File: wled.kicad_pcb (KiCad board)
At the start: 2 copper layers, 310 x 282.6 mm, 12 parts, among them J0 Screw_Terminal_01x02, J1 Signal_Output_01, J3 1Wire_output_02, J4 1Wire_output_01, J5 I2C_output_01, SW1 Button_01, SW2 Button_Reset, U1 NodeMCU_1.0_(ESP-12E)

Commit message: feat: Updated PCB design
This is a Release Candidate version of the board. It still has some issues, and they will be fixed in the next commit
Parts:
- removed C1: Capacitor_1000μF, Capacitor_THT:CP_Radial_D10.0mm_P5.00mm
- J0: value Screw_Terminal_01x02 -> PinHeader_1x02_P2.54mm_Horizontal; footprint TerminalBlock:TerminalBlock_bornier-2_P5.08mm -> Connector_PinHeader_2.54mm:PinHeader_1x02_P2.54mm_Horizontal
- J1: value Signal_Output_01 -> PinHeader_1x03_P2.54mm_Horizontal; footprint TerminalBlock:TerminalBlock_bornier-3_P5.08mm -> Connector_PinHeader_2.54mm:PinHeader_1x03_P2.54mm_Horizontal
- R1: value Resistor_220kΩ -> 220kΩ
- R2: value Resistor_62Ω -> 62Ω
- SW1: value Button_01 -> SW_Push
- SW2: value Button_Reset -> SW_Push
- moved J0 97.9 mm to (82.5, 124.5), turned to 180 degrees
- moved J1 74.4 mm to (153.1, 105.4), turned to 0 degrees
- moved SW2 71.5 mm to (82.2, 115.0), turned to 90 degrees
- moved R1 69.3 mm to (80.6, 101.0), turned to 0 degrees
- moved R2 54.3 mm to (139.7, 105.4), turned to 0 degrees
- moved J4 53.0 mm to (82.6, 78.7), turned to 90 degrees
- moved C2 41.9 mm to (129.5, 109.2), turned to 0 degrees
- moved J3 39.7 mm to (82.6, 87.4), turned to 90 degrees
- moved J5 37.1 mm to (111.8, 85.1), turned to 90 degrees
- moved U1 33.5 mm to (105.4, 113.0), turned to 0 degrees
- moved SW1 31.7 mm to (128.6, 87.4)
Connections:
- net Net-(C2-Pad2) renamed SIG_OUT_3V3DC
- net Net-(C2-Pad8) renamed SIG_OUT_RAW
- net Net-(J5-Pad3) renamed I2C_SCL
- net Net-(J5-Pad4) renamed I2C_SDA
- net Net-(R1-Pad1) renamed RST_PUP
- net Net-(SW1-Pad2) renamed BTN_DATA
- C2 pad 10: Net-(C1-Pad2) -> GND
- C2 pad 3: Net-(C2-Pad3) -> 3V3DC
- C2 pad 4: Net-(C2-Pad4) -> GND
- C2 pad 9: Net-(C1-Pad1) -> 5VDC
- J0 pad 1: Net-(C1-Pad1) -> GND
- J0 pad 2: Net-(C1-Pad2) -> 5VDC
- J1 pad 1: Net-(C1-Pad1) -> GND
- J1 pad 2: Net-(J1-Pad2) -> 5VDC
- J1 pad 3: Net-(C1-Pad2) -> SIG_OUT_5VDC
- J3 pad 1: Net-(J3-Pad1) -> GND
- J3 pad 2: Net-(J3-Pad2) -> 3V3DC
- J3 pad 3: Net-(J3-Pad3) -> 1WIRE_02
- J4 pad 1: Net-(J3-Pad1) -> GND
- J4 pad 2: Net-(J4-Pad2) -> 3V3DC
- J4 pad 3: Net-(J3-Pad3) -> 1WIRE_01
- J5 pad 1: Net-(J3-Pad1) -> GND
- J5 pad 2: Net-(J3-Pad3) -> 3V3DC
- R1 pad 2: Net-(J3-Pad3) -> 3V3DC
- R2 pad 2: Net-(J1-Pad2) -> SIG_OUT_5VDC
- SW1 pad 1: Net-(J3-Pad3) -> 3V3DC
- SW2 pad 1: Net-(C1-Pad2) -> GND
- U1 pad 10: Net-(J3-Pad1) -> GND
- U1 pad 11: Net-(J3-Pad3) -> 3V3DC
- U1 pad 14: Net-(C1-Pad2) -> GND
- U1 pad 15: Net-(C1-Pad1) -> 5VDC
- U1 pad 17: unconnected-(U1-Pad17) -> GND
- U1 pad 2: unconnected-(U1-Pad2) -> GND
- U1 pad 24: Net-(C2-Pad4) -> GND
- U1 pad 25: Net-(C2-Pad3) -> 3V3DC
- U1 pad 4: Net-(J3-Pad2) -> 1WIRE_02
- U1 pad 5: Net-(J4-Pad2) -> 1WIRE_01
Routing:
- net 3V3DC: track 0.00 -> 122.4 mm
- net Net-(C1-Pad2): track 105.7 -> 0.00 mm
- net 5VDC: track 0.00 -> 94.9 mm
- net BTN_DATA: track 100.9 -> 11.0 mm
- net Net-(C1-Pad1): track 87.8 -> 0.00 mm
- net Net-(J3-Pad3): track 59.3 -> 0.00 mm
- net I2C_SDA: track 74.7 -> 18.1 mm
- net I2C_SCL: track 67.1 -> 16.6 mm
- net 1WIRE_01: track 0.00 -> 43.8 mm
- net Net-(J3-Pad1): track 41.0 -> 0.00 mm
- net 1WIRE_02: track 0.00 -> 26.3 mm
- net Net-(J3-Pad2): track 19.6 -> 0.00 mm
- net Net-(J4-Pad2): track 12.0 -> 0.00 mm
- net Net-(J1-Pad2): track 11.4 -> 0.00 mm
- net RST_PUP: track 12.3 -> 22.7 mm
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- added copper zone on F.Cu, net GND
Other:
- board size 310 x 282.6 mm -> 77.6 x 71.8 mm
- board text added: "sowi.tech ohw-wled v1.0-RC"
- board text removed: "sowi.tech WLED@ESP32 v0.1"

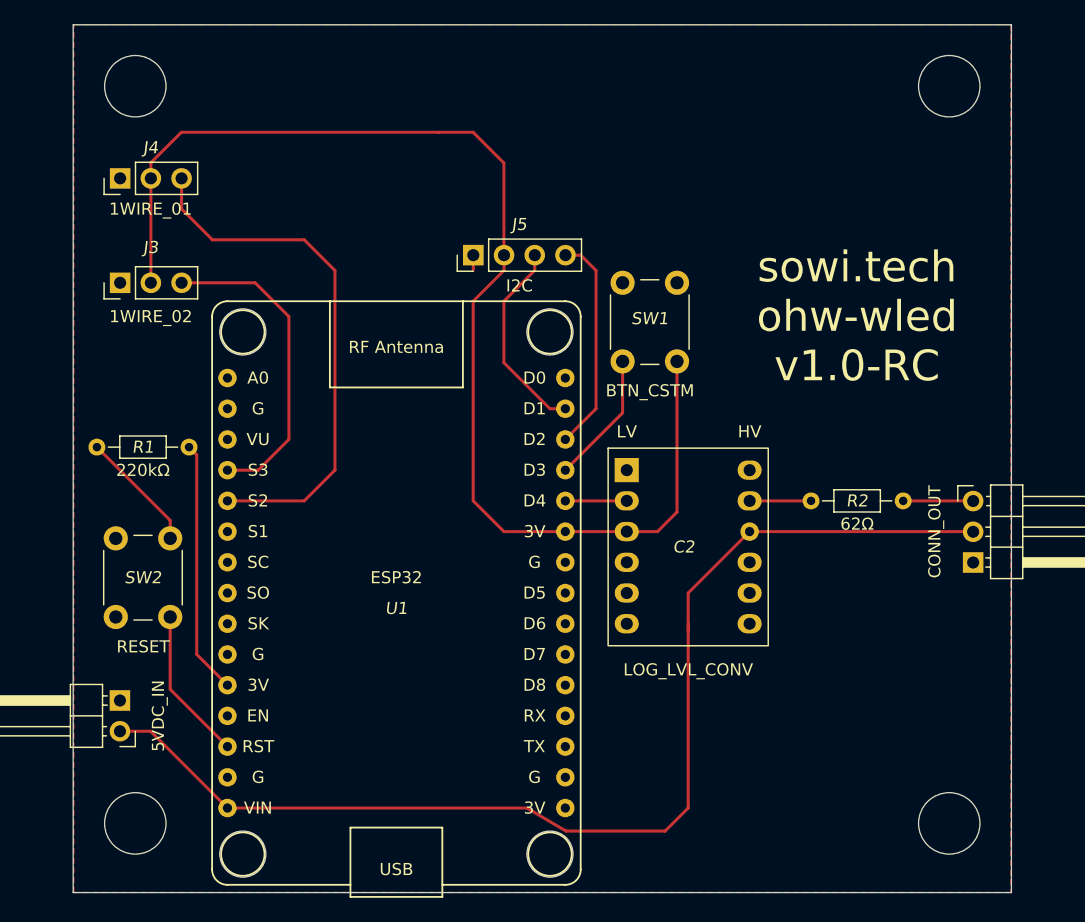
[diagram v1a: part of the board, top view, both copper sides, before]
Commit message: feat: Migrated project to KiCad 7.0
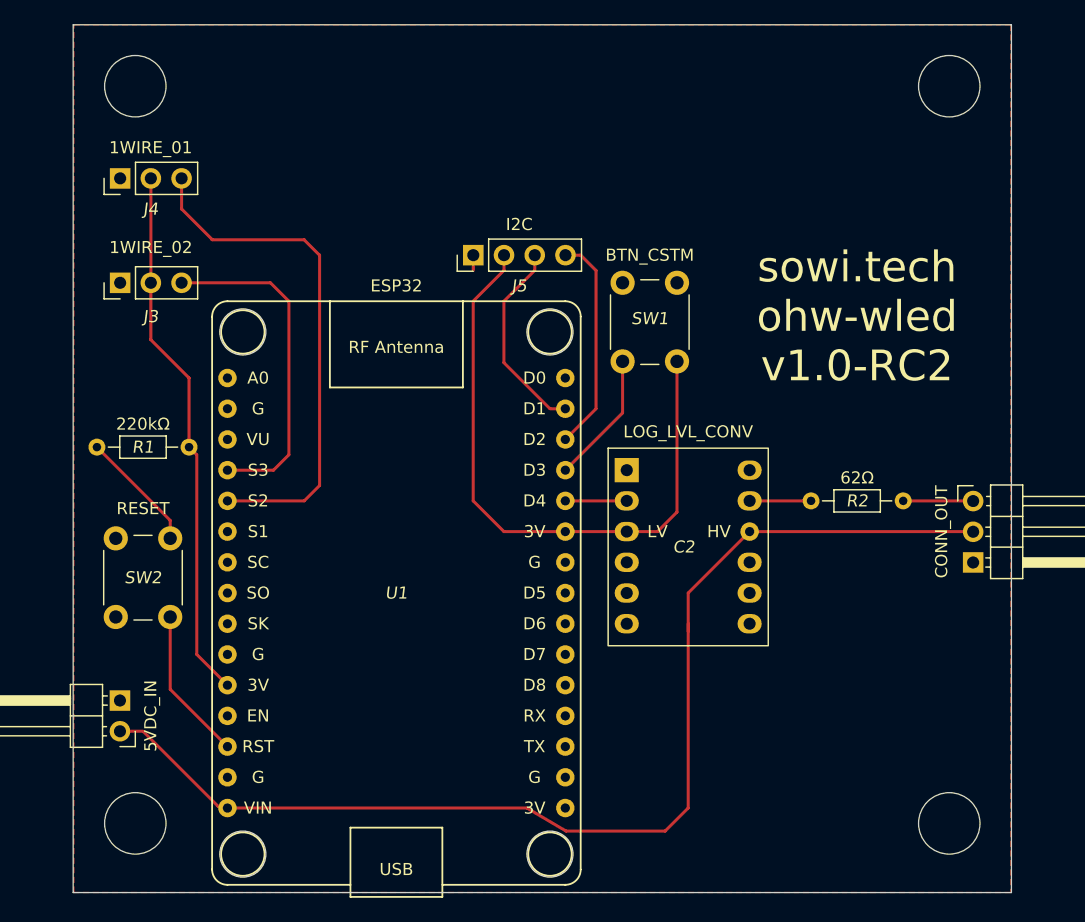
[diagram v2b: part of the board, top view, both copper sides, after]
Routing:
- net 3V3DC: track 122.4 -> 97.1 mm
- net 1WIRE_02: track 26.3 -> 27.8 mm
- net 1WIRE_01: track 43.8 -> 42.8 mm
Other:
- board text added: "sowi.tech ohw-wled v1.0-RC2"
- board text removed: "sowi.tech ohw-wled v1.0-RC"
